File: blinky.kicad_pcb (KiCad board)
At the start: 4 copper layers, 50 x 50 mm, 126 parts, among them J1 Power, J2 Skedd, U1 STM32G030C6Tx, U2 BQ25570

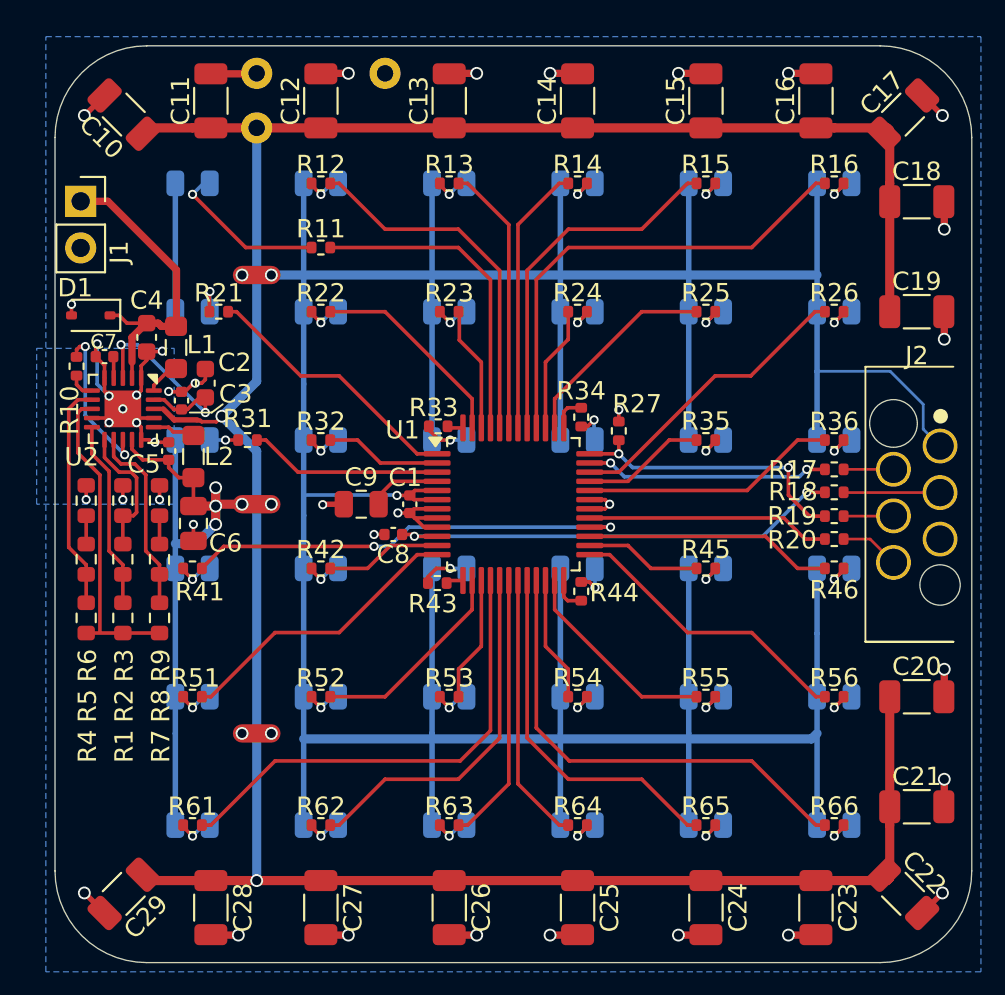
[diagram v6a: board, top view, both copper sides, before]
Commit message: Believe the datasheet not the website
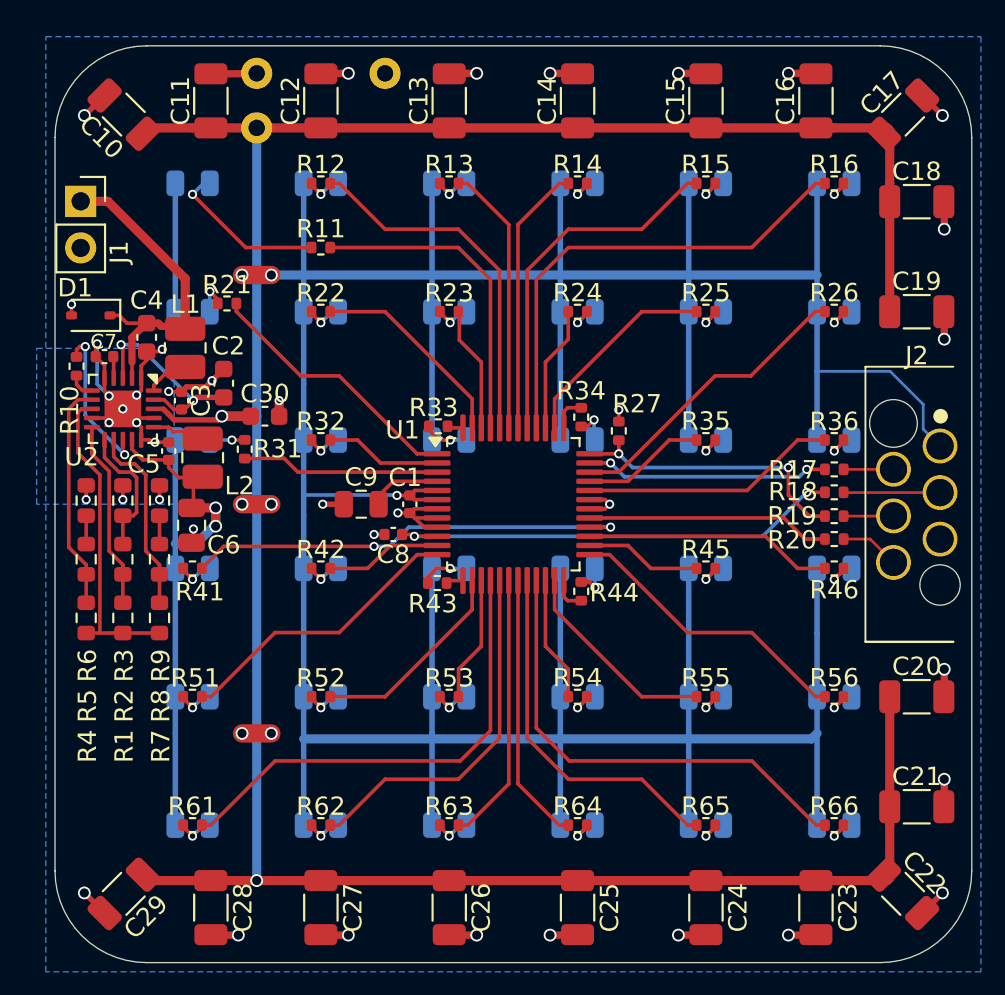
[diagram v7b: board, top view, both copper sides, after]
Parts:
- added C30: 10u, Capacitor_SMD:C_0603_1608Metric, F.Cu at (86.5, 95.2)
- L1, L2: footprint Inductor_SMD:L_0805_2012Metric_Pad1.05x1.20mm_HandSolder -> Parts:L_1008_2520Metric-Adjusted
- moved C2 1.00 mm to (84.2, 93.4)
- moved R21 0.64 mm to (84.4, 89.0)
- moved R31 0.52 mm to (85.3, 97.0), turned to -90 degrees
- moved L2 0.51 mm to (83.1, 97.5)
- moved L1 0.50 mm to (82.1, 91.5)
- moved C6 0.14 mm to (82.5, 101.2)
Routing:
- net +3V3: track 271.3 -> 267.6 mm, vias 10 -> 9
- net /VBatt: track 147.5 -> 149.3 mm
- net GND: track 62.0 -> 63.5 mm, vias 39 -> 40
- net /VStor: track 11.8 -> 11.2 mm
